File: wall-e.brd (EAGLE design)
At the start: 61.3 x 51.1 mm, 71 parts, among them IC1 VREG-TS1117CW-3V3, T1 BC847, U1 TSM2306CX, U2 TSM2306CX, U3 TSM2306CX, U4 TSM2306CX, U5 TSM2306CX, U6 TSM2306CX, U7 TSM2306CX, U8 LM293AD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

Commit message: Routing
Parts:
- moved D6 14.0 mm to (92.5, 59.1), turned to 270 degrees
- moved U4 12.3 mm to (91.1, 56.6), turned to 90 degrees
- moved R19 12.3 mm to (108.6, 46.8), flipped to the top
- moved D7 11.7 mm to (100.8, 65.8), flipped to the bottom, turned to 270 degrees
- moved C15 9.54 mm to (111.2, 65.5), turned to 180 degrees
- moved D3 7.95 mm to (100.6, 57.9), turned to 180 degrees
- moved U3 7.32 mm to (91.8, 44.4)
- moved U2 7.17 mm to (94.7, 48.8)
- moved U1 4.27 mm to (91.9, 52.4)
- moved D1 3.39 mm to (95.3, 52.2), turned to 90 degrees
- turned LD1 to 180 degrees
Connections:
- net BUTTON1: now also U$1.11; no longer U$1.10
- net BUTTON2: now also U$1.10; no longer U$1.11
- net JACK: now also U$1.15; no longer U$1.14
- net N$7: now also PNEUMATIC.6; no longer PNEUMATIC.5
- net VALVE1: now also U$1.20; no longer U$1.15
- net VALVE2: now also U$1.19; no longer U$1.18
- net VALVE3: now also U$1.18; no longer U$1.19
- net VALVE4: now also U$1.14; no longer U$1.20
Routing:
- net CODEUSE1_TIM: track 0.00 -> 121.3 mm, vias 0 -> 2
- net CODEUSE1: track 0.00 -> 120.8 mm, vias 0 -> 2
- net CODEUSE2_TIM: track 0.00 -> 115.0 mm, vias 0 -> 4
- net CODEUSE2: track 0.00 -> 110.6 mm, vias 0 -> 4
- net BUTTON3: track 0.00 -> 81.2 mm
- net MCU_RESET: track 28.9 -> 89.6 mm, vias 2 -> 3
- net GND: track 95.7 -> 54.1 mm, vias 5 -> 3
- net BUTTON1: track 0.00 -> 35.1 mm, vias 0 -> 2
- net BUTTON2: track 0.00 -> 32.7 mm, vias 0 -> 2
- net N$23: track 0.00 -> 30.4 mm, vias 0 -> 4
- net JACK: track 0.00 -> 27.9 mm, vias 0 -> 2
- net LED4: track 22.5 -> 0.00 mm, vias 1 -> 0
- net +5V: track 45.0 -> 23.4 mm, vias 2 -> 1
- net N$7: track 0.00 -> 19.8 mm
- net N$9: track 3.64 -> 22.1 mm, vias 0 -> 2
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
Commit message: Routing
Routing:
- net +5V: track 23.4 -> 214.3 mm, vias 1 -> 15
- net +12V: track 8.09 -> 173.7 mm, vias 1 -> 5
- net +3V3: track 57.9 -> 150.7 mm, vias 6 -> 11
- net LED4: track 0.00 -> 23.0 mm, vias 0 -> 1
- net MOTOR2_PWM: track 4.80 -> 24.2 mm, vias 0 -> 2
- net N$14: track 0.00 -> 18.2 mm
- net N$19: track 10.9 -> 28.6 mm, vias 2 -> 3
- net N$23: track 30.4 -> 46.2 mm, vias 4 -> 3
- net N$5: track 2.40 -> 17.6 mm, vias 0 -> 2
- net N$25: track 4.91 -> 15.4 mm, vias 0 -> 1
- net LED1: track 18.7 -> 24.1 mm
- net VALVE2: track 5.58 -> 8.98 mm, vias 0 -> 2
- net VALVE1: track 13.0 -> 14.7 mm, vias 2 -> 0
- net MCU_RESET: track 89.6 -> 91.0 mm
- net BUTTON2: track 32.7 -> 31.7 mm
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- added copper zone on layer 1, net GND
- added copper zone on layer 16, net GND

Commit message: Routing
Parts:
- moved C14 0.67 mm to (82.6, 49.4)
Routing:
- net GND: track 53.4 -> 126.4 mm, vias 3 -> 30
- net +3V3: track 150.7 -> 157.1 mm, vias 11 -> 10
- net N$11: track 0.00 -> 5.32 mm, vias 0 -> 1
- net N$25: track 15.4 -> 19.6 mm, vias 1 -> 3
- net N$19: track 28.6 -> 32.0 mm, vias 3 -> 2
- net VALVE1: track 14.7 -> 11.8 mm
- net LED2: track 21.6 -> 23.0 mm
- net MOTOR2_1: track 12.1 -> 13.3 mm
- net N$23: track 46.2 -> 47.2 mm
- net LED1: track 24.1 -> 24.9 mm

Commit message: First DRC
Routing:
- net GND: track 126.4 -> 124.4 mm
- net N$19: track 32.0 -> 31.4 mm, vias 2 -> 3
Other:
- board size 61.3 x 51.1 mm -> 62.3 x 52.7 mm
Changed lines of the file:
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@@
 <board>
 <plain>
-<wire x1="53.15" y1="17.5" x2="114.48" y2="17.61" width="0" layer="20"/>
-<wire x1="114.48" y1="17.61" x2="114.42" y2="68.46" width="0" layer="20"/>
-<wire x1="114.42" y1="68.46" x2="53.39" y2="68.57" width="0" layer="20"/>
-<wire x1="53.39" y1="68.57" x2="53.15" y2="17.5" width="0" layer="20"/>
+<wire x1="52.72" y1="16.74" x2="115.05" y2="16.23" width="0" layer="20"/>
+<wire x1="115.05" y1="16.23" x2="114.95" y2="68.77" width="0" layer="20"/>
+<wire x1="114.95" y1="68.77" x2="52.75" y2="68.93" width="0" layer="20"/>
+<wire x1="52.75" y1="68.93" x2="52.72" y2="16.74" width="0" layer="20"/>
 </plain>
 <attributes>
@@
 </polygon>
 <via x="69.33" y="38.54" extent="1-16" drill="0.6" shape="square"/>
-<wire x1="72.02" y1="38.52" x2="74.16" y2="36.38" width="0.4064" layer="16"/>
-<wire x1="74.16" y1="36.38" x2="77.18" y2="36.38" width="0.4064" layer="16"/>
 <via x="105.06" y="23.39" extent="1-16" drill="0.6" shape="square"/>
 <via x="107.88" y="30.02" extent="1-16" drill="0.6" shape="square"/>
@@
 <via x="87.18" y="27" extent="1-16" drill="0.6" shape="square"/>
 <via x="85.91" y="31.7" extent="1-16" drill="0.6" shape="square"/>
+<wire x1="72.02" y1="38.52" x2="73.6" y2="36.94" width="0.4064" layer="16"/>
+<wire x1="73.6" y1="36.94" x2="75.45" y2="36.94" width="0.4064" layer="16"/>
 <wire x1="89.12" y1="55.44" x2="88.5198" y2="55.31" width="0" layer="19" extent="1-1"/>
+<wire x1="72.02" y1="38.52" x2="69.33" y2="38.54" width="0" layer="19" extent="16-16"/>
 </signal>
 <signal name="+5V">
@@
 <wire x1="64.57" y1="34.86" x2="64.57" y2="34.505" width="0.4064" layer="1"/>
 <wire x1="64.57" y1="34.505" x2="68.9362" y2="34.505" width="0.4064" layer="1"/>
-<wire x1="73.8638" y1="34.505" x2="68.9362" y2="34.505" width="0.4064" layer="16"/>
-<wire x1="73.8638" y1="34.505" x2="77.18" y2="34.505" width="0.4064" layer="16"/>
 <wire x1="77.18" y1="34.505" x2="77.18" y2="34.48" width="0.4064" layer="16"/>
-<wire x1="77.18" y1="34.48" x2="73.8638" y2="34.48" width="0.4064" layer="16"/>
+<wire x1="73.8638" y1="34.505" x2="73.8638" y2="34.48" width="0.4064" layer="16"/>
+<wire x1="76.07" y1="34.48" x2="77.18" y2="34.48" width="0.4064" layer="16"/>
+<wire x1="76.07" y1="34.48" x2="73.8638" y2="34.48" width="0.4064" layer="16"/>
 <wire x1="73.8638" y1="34.48" x2="73.8638" y2="34.505" width="0.4064" layer="16"/>
+<wire x1="68.9362" y1="34.505" x2="75.105" y2="34.505" width="0.4064" layer="1"/>
+<wire x1="75.105" y1="34.505" x2="75.62" y2="35.02" width="0.4064" layer="1"/>
+<via x="75.62" y="35.02" extent="1-16" drill="0.6" shape="square"/>
+<wire x1="75.62" y1="35.02" x2="75.62" y2="34.93" width="0.4064" layer="16"/>
+<wire x1="75.62" y1="34.93" x2="76.07" y2="34.48" width="0.4064" layer="16"/>
 </signal>
 <signal name="N$20">
@@
 <wire x1="70.77" y1="35.78" x2="72.46" y2="35.78" width="0.4064" layer="1"/>
 <wire x1="72.46" y1="35.78" x2="72.47" y2="35.77" width="0.4064" layer="1"/>
-<via x="72.47" y="35.77" extent="1-16" drill="0.6" shape="square"/>
-<wire x1="72.47" y1="35.77" x2="73.8588" y2="35.77" width="0.4064" layer="16"/>
 <wire x1="73.8588" y1="35.77" x2="73.8638" y2="35.775" width="0.4064" layer="16"/>
+<wire x1="72.47" y1="35.77" x2="73.09" y2="35.77" width="0.4064" layer="1"/>
+<via x="73.09" y="35.77" extent="1-16" drill="0.6" shape="square"/>
+<wire x1="73.8638" y1="35.775" x2="73.095" y2="35.775" width="0.4064" layer="16"/>
+<wire x1="73.095" y1="35.775" x2="73.09" y2="35.77" width="0.4064" layer="16"/>
 </signal>
 <signal name="N$23">
@@
 <contactref element="X5" pad="2"/>
 <contactref element="U$1" pad="38"/>
-<wire x1="78.05" y1="51.78" x2="75.3" y2="51.78" width="0.4064" layer="1"/>
+<wire x1="78.05" y1="51.78" x2="75.3" y2="51.78" width="0.3048" layer="1"/>
 <wire x1="75.3" y1="51.78" x2="75.3" y2="55.25" width="0.4064" layer="1"/>
 <wire x1="75.3" y1="55.25" x2="72.72" y2="55.25" width="0.4064" layer="1"/>

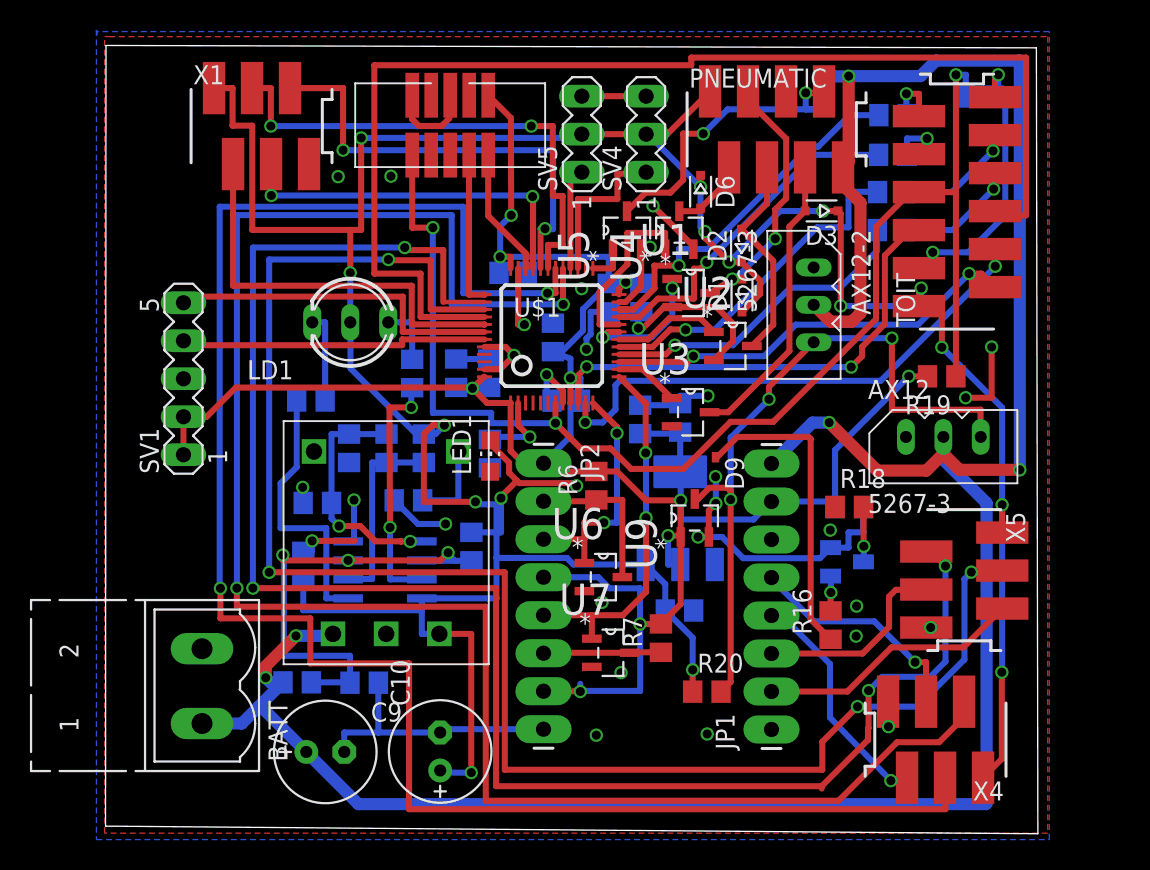
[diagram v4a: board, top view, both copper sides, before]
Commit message: Correction of the DRC errors
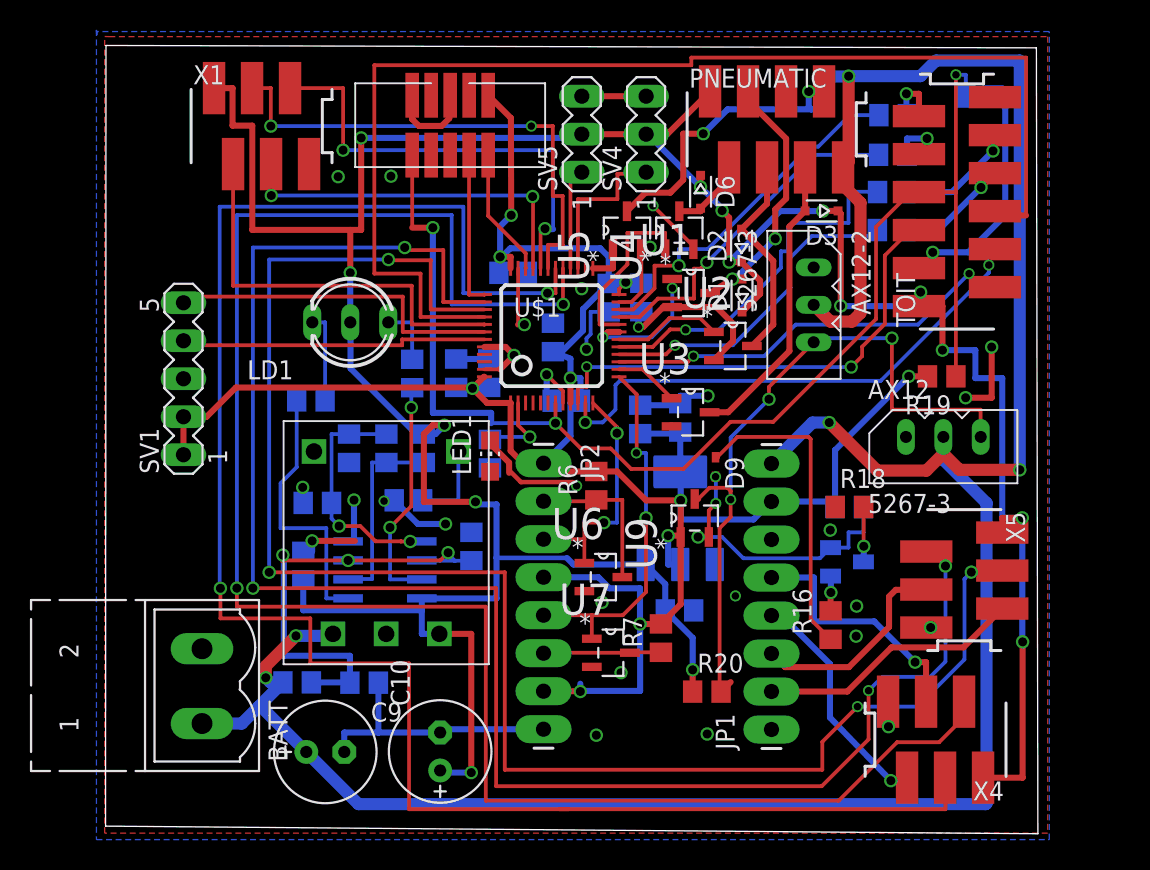
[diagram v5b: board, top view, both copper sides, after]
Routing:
- net GND: track 124.4 -> 116.1 mm
- net +5V: track 214.3 -> 220.0 mm
- net MOTOR1_1: track 15.4 -> 17.1 mm
- net LED2: track 23.0 -> 24.4 mm
- net N$9: track 22.1 -> 20.8 mm
- net N$23: track 47.2 -> 48.2 mm
- net N$16: track 16.5 -> 15.6 mm
- net MOTOR2_1: track 13.3 -> 14.1 mm
- net LED1: track 24.9 -> 24.3 mm
- net CODEUSE1: track 120.8 -> 121.4 mm
- net N$4: track 8.11 -> 7.55 mm

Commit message: Some corrections
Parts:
- moved JP1 0.12 mm to (97.2, 23.3)
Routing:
- net N$18: track 0.00 -> 3.57 mm, vias 0 -> 1
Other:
- board size 62.3 x 52.7 mm -> 62.2 x 51.9 mm
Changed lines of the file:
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@@
 <layer number="43" name="vRestrict" color="2" fill="10" visible="yes" active="yes"/>
 <layer number="44" name="Drills" color="7" fill="1" visible="no" active="yes"/>
-<layer number="45" name="Holes" color="7" fill="1" visible="no" active="yes"/>
+<layer number="45" name="Holes" color="7" fill="1" visible="yes" active="yes"/>
 <layer number="46" name="Milling" color="3" fill="1" visible="no" active="yes"/>
 <layer number="47" name="Measures" color="7" fill="1" visible="no" active="yes"/>
@@
 <board>
 <plain>
-<wire x1="52.72" y1="16.74" x2="115.05" y2="16.23" width="0" layer="20"/>
-<wire x1="115.05" y1="16.23" x2="114.95" y2="68.77" width="0" layer="20"/>
-<wire x1="114.95" y1="68.77" x2="52.75" y2="68.93" width="0" layer="20"/>
-<wire x1="52.75" y1="68.93" x2="52.72" y2="16.74" width="0" layer="20"/>
+<wire x1="52.75" y1="17" x2="115" y2="17" width="0" layer="20"/>
+<wire x1="115" y1="17" x2="115" y2="68.9" width="0" layer="20"/>
+<wire x1="115" y1="68.9" x2="52.75" y2="68.9" width="0" layer="20"/>
+<wire x1="52.75" y1="68.9" x2="52.75" y2="17" width="0" layer="20"/>
+<hole x="55.5" y="65" drill="3.2"/>
+<hole x="55.5" y="36" drill="3.2"/>
+<hole x="89.65" y="23.03" drill="3.2"/>
 </plain>
 <attributes>
@@
 </element>
 <element name="X1" library="con-amp" package="SMDTOP6" value="" x="63.15" y="63.54"/>
-<element name="JP1" library="SparkFun" package="1X08_LONGPADS" value="" x="97.24" y="23.2" rot="R90"/>
+<element name="JP1" library="SparkFun" package="1X08_LONGPADS" value="" x="97.24" y="23.32" rot="R90"/>
 <element name="JP2" library="SparkFun" package="1X08_LONGPADS" value="" x="82" y="41" rot="R270"/>
 <element name="X4" library="con-amp" package="SMDTOP6" value="" x="108.21" y="22.52" rot="R180"/>
@@
 <wire x1="83.8" y1="47.99" x2="82.63" y2="48.46" width="0.4064" layer="16"/>
 <wire x1="83.8" y1="47.99" x2="83.8" y2="46.7" width="0.4064" layer="16"/>
-<wire x1="101.12" y1="38.44" x2="97.24" y2="38.44" width="0.4064" layer="16"/>
+<wire x1="101.12" y1="38.44" x2="97.24" y2="38.56" width="0.4064" layer="16"/>
 <wire x1="101.12" y1="38.44" x2="101.49" y2="38.07" width="0.4064" layer="16"/>
 <wire x1="101.49" y1="38.07" x2="101.49" y2="41.88" width="0.4064" layer="16"/>
@@
 <wire x1="91.14" y1="40.429" x2="91.1702" y2="40.429" width="0.4064" layer="16"/>
 <wire x1="91.1702" y1="38.52" x2="91.1702" y2="40.429" width="0.4064" layer="16"/>
-<wire x1="97.24" y1="38.44" x2="96.04" y2="37.24" width="0.4064" layer="16"/>
+<wire x1="97.24" y1="38.56" x2="96.04" y2="37.24" width="0.4064" layer="16"/>
 <wire x1="96.04" y1="37.24" x2="91.1702" y2="37.24" width="0.4064" layer="16"/>
 <wire x1="91.1702" y1="37.24" x2="91.1702" y2="38.52" width="0.4064" layer="16"/>
@@
 <wire x1="111.62" y1="38.34" x2="108.73" y2="41.23" width="0.8128" layer="16"/>
 <wire x1="108.73" y1="41.23" x2="108.73" y2="42.76" width="0.8128" layer="16"/>
-<wire x1="97.24" y1="40.98" x2="99.98" y2="43.72" width="0.8128" layer="16"/>
+<wire x1="97.24" y1="41.1" x2="99.98" y2="43.72" width="0.8128" layer="16"/>
 <wire x1="99.98" y1="43.72" x2="101.1" y2="43.72" width="0.8128" layer="16"/>
 <via x="101.1" y="43.72" extent="1-16" drill="0.6" shape="square"/>
@@
 <wire x1="106.84" y1="27.7" x2="104.11" y2="30.43" width="0.4064" layer="16"/>
 <wire x1="100.08" y1="30.43" x2="104.11" y2="30.43" width="0.4064" layer="16"/>
-<wire x1="97.24" y1="33.27" x2="97.24" y2="33.36" width="0.4064" layer="16"/>
-<wire x1="97.24" y1="33.36" x2="100.08" y2="33.36" width="0.4064" layer="16"/>
+<wire x1="97.24" y1="33.27" x2="97.24" y2="33.48" width="0.4064" layer="16"/>
+<wire x1="97.24" y1="33.48" x2="100.08" y2="33.36" width="0.4064" layer="16"/>
 <wire x1="100.08" y1="33.36" x2="100.08" y2="30.43" width="0.4064" layer="16"/>
 </signal>
@@
 <wire x1="101.15" y1="24" x2="101.15" y2="27.58" width="0.4064" layer="16"/>
 <wire x1="101.15" y1="27.58" x2="97.91" y2="30.82" width="0.4064" layer="16"/>
-<wire x1="97.91" y1="30.82" x2="97.24" y2="30.82" width="0.4064" layer="16"/>
+<wire x1="97.91" y1="30.82" x2="97.24" y2="30.94" width="0.4064" layer="16"/>
 <wire x1="106.305" y1="19.98" x2="106.305" y2="19.78" width="0.4064" layer="1"/>
 <wire x1="106.305" y1="19.78" x2="105.22" y2="19.78" width="0.4064" layer="1"/>
@@
 <wire x1="105.55" y1="32.54" x2="107.575" y2="32.54" width="0.4064" layer="1"/>
 <wire x1="107.575" y1="32.54" x2="107.59" y2="32.555" width="0.4064" layer="1"/>
-<wire x1="97.24" y1="28.28" x2="98.15" y2="27.37" width="0.4064" layer="1"/>
+<wire x1="97.24" y1="28.4" x2="98.15" y2="27.37" width="0.4064" layer="1"/>
 <wire x1="98.15" y1="27.37" x2="102.42" y2="27.37" width="0.4064" layer="1"/>
 <wire x1="102.42" y1="27.37" x2="105.1" y2="30.05" width="0.4064" layer="1"/>
@@
 <contactref element="JP1" pad="2"/>
 <contactref element="X5" pad="5"/>
-<wire x1="97.24" y1="25.74" x2="102.31" y2="25.74" width="0.4064" layer="1"/>
+<wire x1="97.24" y1="25.86" x2="102.31" y2="25.74" width="0.4064" layer="1"/>
 <wire x1="102.31" y1="25.74" x2="105.26" y2="28.69" width="0.4064" layer="1"/>
 <wire x1="105.26" y1="28.69" x2="110.075" y2="28.69" width="0.4064" layer="1"/>
@@
 <contactref element="R1" pad="2"/>
 <contactref element="LED1" pad="A"/>
-<wire x1="78.43" y1="40.43" x2="78.42" y2="40.69" width="0" layer="19" extent="1-16"/>
+<wire x1="78.42" y1="40.69" x2="77.37" y2="40.69" width="0.254" layer="16"/>
+<wire x1="77.37" y1="40.69" x2="77.37" y2="39.83" width="0.254" layer="16"/>
+<via x="77.37" y="39.83" extent="1-16" drill="0.5" shape="square"/>
+<wire x1="77.37" y1="39.83" x2="78.43" y2="39.83" width="0.254" layer="1"/>
+<wire x1="78.43" y1="39.83" x2="78.43" y2="40.43" width="0.254" layer="1"/>
 </signal>
 <signal name="N$22">
